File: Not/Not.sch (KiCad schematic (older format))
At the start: 9 parts, among them J1 In1, J2 Out, J3 Thru1

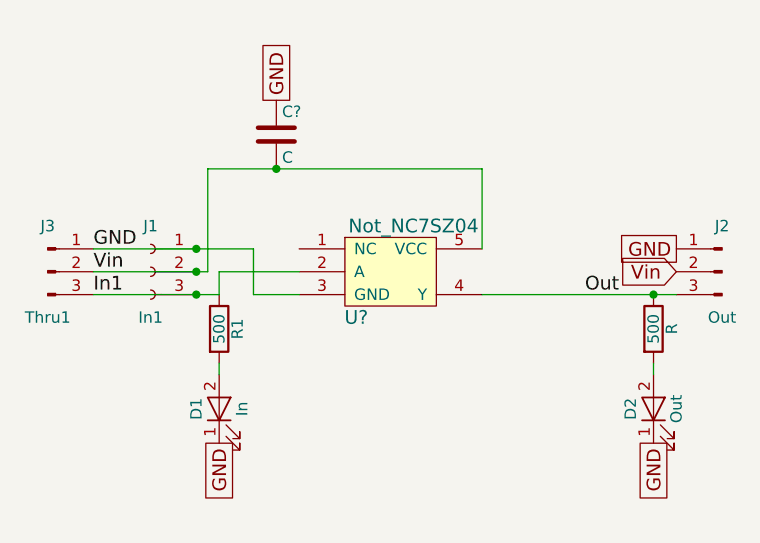
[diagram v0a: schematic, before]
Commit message: Made XOR Board and modified FA
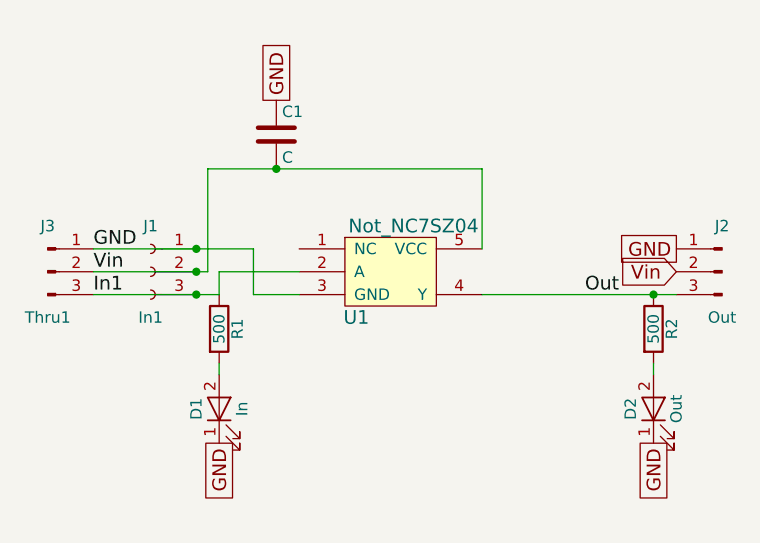
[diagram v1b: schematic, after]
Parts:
- C1: renamed from C?; footprint (none) -> Capacitors_SMD:C_0603_HandSoldering
- D1, D2: footprint (none) -> LEDs:LED_0603_HandSoldering
- J1: footprint (none) -> Socket_Strips:Socket_Strip_Angled_1x03_Pitch2.54mm
- J2, J3: footprint (none) -> Pin_Headers:Pin_Header_Angled_1x03_Pitch2.54mm
- R1: footprint (none) -> Resistors_SMD:R_0603_HandSoldering
- R2: renamed from R; footprint (none) -> Resistors_SMD:R_0603_HandSoldering
- U1: renamed from U?; footprint (none) -> Logic Blocks:SC_70_1.25mm
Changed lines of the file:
@@
 F 0 "J2" H 6900 4550 50  0000 C CNN
 F 1 "Out" H 6900 4150 50  0000 C CNN
-F 2 "" H 6900 4350 50  0001 C CNN
+F 2 "Pin_Headers:Pin_Header_Angled_1x03_Pitch2.54mm" H 6900 4350 50  0001 C CNN
 F 3 "" H 6900 4350 50  0001 C CNN
 	1    6900 4350
@@
 F 0 "J1" H 4400 4550 50  0000 C CNN
 F 1 "In1" H 4400 4150 50  0000 C CNN
-F 2 "" H 4400 4350 50  0001 C CNN
+F 2 "Socket_Strips:Socket_Strip_Angled_1x03_Pitch2.54mm" H 4400 4350 50  0001 C CNN
 F 3 "" H 4400 4350 50  0001 C CNN
 	1    4400 4350
@@
 F 0 "J3" H 3950 4550 50  0000 C CNN
 F 1 "Thru1" H 3950 4150 50  0000 C CNN
-F 2 "" H 3950 4350 50  0001 C CNN
+F 2 "Pin_Headers:Pin_Header_Angled_1x03_Pitch2.54mm" H 3950 4350 50  0001 C CNN
 F 3 "" H 3950 4350 50  0001 C CNN
 	1    3950 4350
@@
 F 0 "D1" H 4700 5050 50  0000 C CNN
 F 1 "In" H 4700 4850 50  0000 C CNN
-F 2 "" H 4700 4950 50  0001 C CNN
+F 2 "LEDs:LED_0603_HandSoldering" H 4700 4950 50  0001 C CNN
 F 3 "" H 4700 4950 50  0001 C CNN
 	1    4700 4950
@@
 F 0 "D2" H 6600 5050 50  0000 C CNN
 F 1 "Out" H 6600 4850 50  0000 C CNN
-F 2 "" H 6600 4950 50  0001 C CNN
+F 2 "LEDs:LED_0603_HandSoldering" H 6600 4950 50  0001 C CNN
 F 3 "" H 6600 4950 50  0001 C CNN
 	1    6600 4950
@@
 $EndComp
 $Comp
-L R R
+L R R2
 U 1 1 5AF0BC16
 P 6600 4600
-F 0 "R" V 6680 4600 50  0000 C CNN
+F 0 "R2" V 6680 4600 50  0000 C CNN
 F 1 "500" V 6600 4600 50  0000 C CNN
-F 2 "" V 6530 4600 50  0001 C CNN
+F 2 "Resistors_SMD:R_0603_HandSoldering" V 6530 4600 50  0001 C CNN
 F 3 "" H 6600 4600 50  0001 C CNN
 	1    6600 4600
@@
 F 0 "R1" V 4780 4600 50  0000 C CNN
 F 1 "500" V 4700 4600 50  0000 C CNN
-F 2 "" V 4630 4600 50  0001 C CNN
+F 2 "Resistors_SMD:R_0603_HandSoldering" V 4630 4600 50  0001 C CNN
 F 3 "" H 4700 4600 50  0001 C CNN
 	1    4700 4600
@@
 Out
 $Comp
-L Not_NC7SZ04 U?
+L Not_NC7SZ04 U1
 U 1 1 5AF1E8CB
 P 5250 4500
-F 0 "U?" H 5300 4450 60  0000 C CNN
+F 0 "U1" H 5300 4450 60  0000 C CNN
 F 1 "Not_NC7SZ04" H 5550 4850 60  0000 C CNN
-F 2 "" H 5050 3800 60  0001 C CNN
+F 2 "Logic Blocks:SC_70_1.25mm" H 5050 3800 60  0001 C CNN
 F 3 "" H 5050 3800 60  0001 C CNN
 	1    5250 4500
@@
 Connection ~ 4600 4350
 $Comp
-L C C?
+L C C1
 U 1 1 5AF1E96C
 P 4950 3750
-F 0 "C?" H 4975 3850 50  0000 L CNN
+F 0 "C1" H 4975 3850 50  0000 L CNN
 F 1 "C" H 4975 3650 50  0000 L CNN
-F 2 "" H 4988 3600 50  0001 C CNN
+F 2 "Capacitors_SMD:C_0603_HandSoldering" H 4988 3600 50  0001 C CNN
 F 3 "" H 4950 3750 50  0001 C CNN
 	1    4950 3750
